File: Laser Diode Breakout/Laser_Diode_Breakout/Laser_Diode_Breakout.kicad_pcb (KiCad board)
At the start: 2 copper layers, 29.2 x 35.6 mm, 8 parts, among them Q1 BSS138, Q2 BSS138

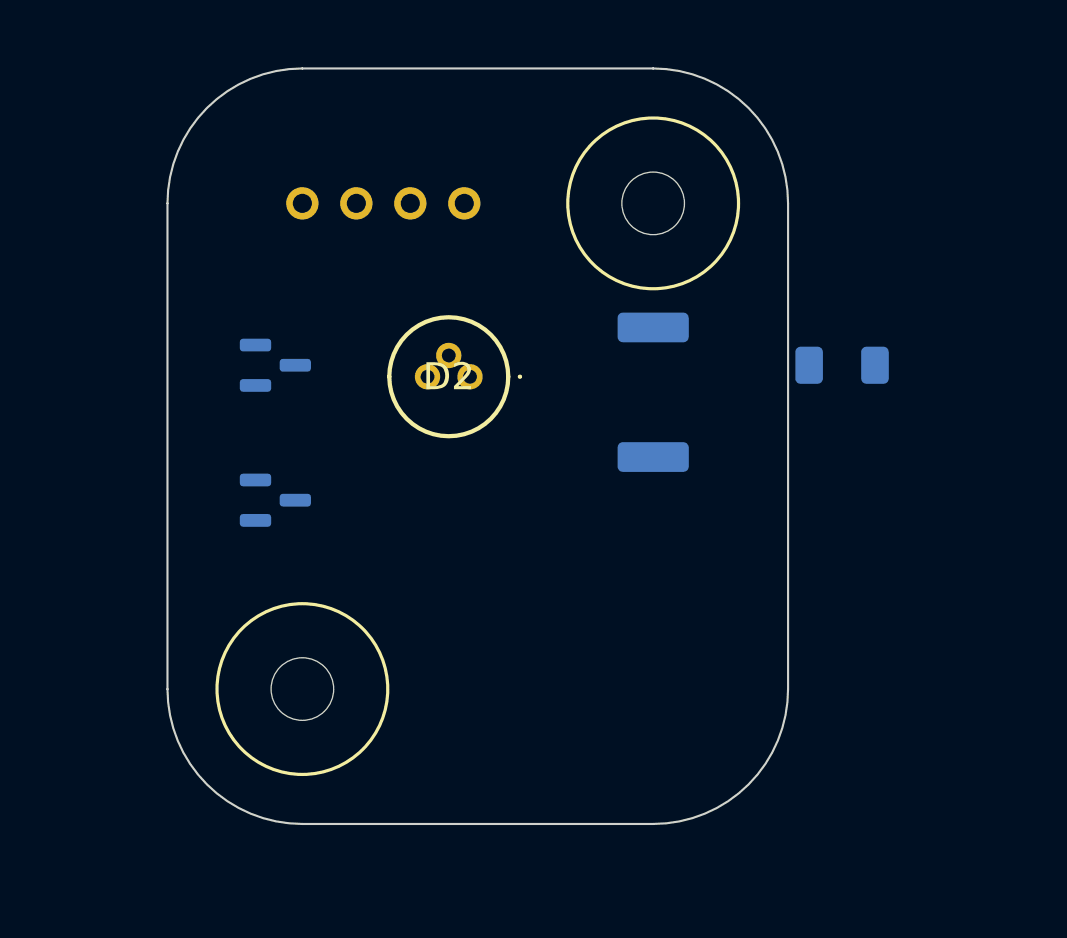
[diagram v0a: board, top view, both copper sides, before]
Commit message: finished adding footprints to laser diode breakout
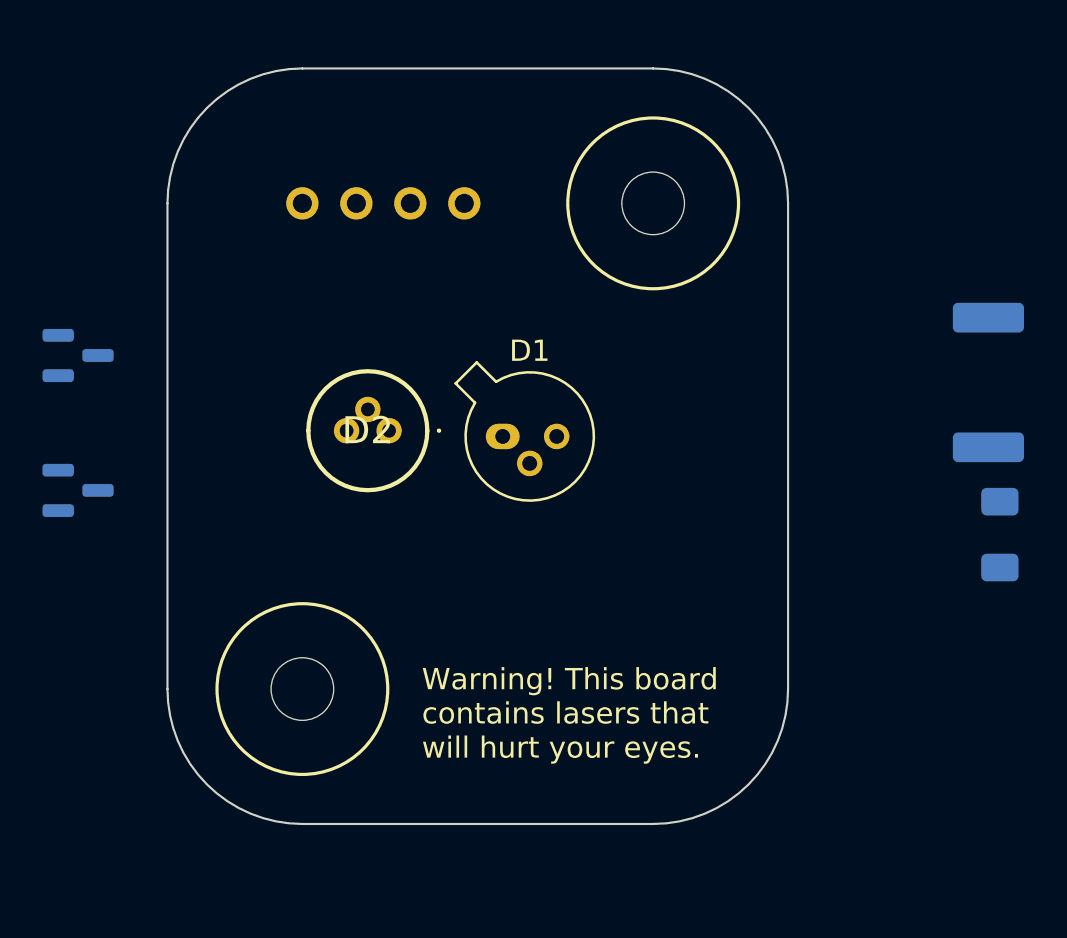
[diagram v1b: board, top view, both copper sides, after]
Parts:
- added D1: 785nm Laser Diode, Package_TO_SOT_THT:TO-18-3, F.Cu at (45.7, 47.0)
- moved R1 15.8 mm to (68.6, 44.5)
- moved R2 10.9 mm to (69.1, 51.6), turned to -90 degrees
- moved Q1 9.30 mm to (25.7, 43.2)
- moved Q2 9.30 mm to (25.7, 49.5)
- moved D2 4.58 mm to (40.4, 46.7)
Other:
- board text added: "Warning! This board contains lasers that will hurt your eyes."
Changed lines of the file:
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@@
   (net 7 "Net-(D1-K)")
   (net 8 "Net-(D1-A)")
+  (footprint "Package_TO_SOT_THT:TO-18-3" (layer "F.Cu")
+    (at 45.72 46.99)
+    (descr "TO-18-3")
+    (tags "TO-18-3")
+    (property "Sheetfile" "Laser_Diode_Breakout.kicad_sch")
+    (property "Sheetname" "")
+    (property "ki_description" "Light emitting diode")
+    (property "ki_keywords" "LED diode")
+    (attr through_hole)
+    (fp_text reference "D1" (at 1.27 -4.02) (layer "F.SilkS")
+        (effects (font (size 1 1) (thickness 0.15)))
+    )
+    (fp_text value "785nm Laser Diode" (at -17.78 3.56) (layer "F.Fab")
+        (effects (font (size 1 1) (thickness 0.15)))
+    )
+    (fp_text user "${REFERENCE}" (at 1.27 -4.02) (layer "F.Fab")
+        (effects (font (size 1 1) (thickness 0.15)))
+    )
+    (fp_line (start -2.214448 -2.494499) (end -1.302281 -1.582331)
+      (stroke (width 0.12) (type solid)) (layer "F.SilkS"))
+    (fp_line (start -1.224499 -3.484448) (end -2.214448 -2.494499)
+      (stroke (width 0.12) (type solid)) (layer "F.SilkS"))
+    (fp_line (start -0.312331 -2.572281) (end -1.224499 -3.484448)
+      (stroke (width 0.12) (type solid)) (layer "F.SilkS"))
+    (fp_arc (start -0.312331 -2.572281) (mid 3.405374 2.135551) (end -1.30215 -1.582544)
+      (stroke (width 0.12) (type solid)) (layer "F.SilkS"))
+    (fp_line (start -2.23 -3.5) (end -2.23 3.15)
+      (stroke (width 0.05) (type solid)) (layer "F.CrtYd"))
+    (fp_line (start -2.23 3.15) (end 4.42 3.15)
+      (stroke (width 0.05) (type solid)) (layer "F.CrtYd"))
+    (fp_line (start 4.42 -3.5) (end -2.23 -3.5)
+      (stroke (width 0.05) (type solid)) (layer "F.CrtYd"))
+    (fp_line (start 4.42 3.15) (end 4.42 -3.5)
+      (stroke (width 0.05) (type solid)) (layer "F.CrtYd"))
+    (fp_line (start -1.976616 -2.426372) (end -1.149301 -1.599057)
+      (stroke (width 0.1) (type solid)) (layer "F.Fab"))
+    (fp_line (start -1.156372 -3.246616) (end -1.976616 -2.426372)
+      (stroke (width 0.1) (type solid)) (layer "F.Fab"))
+    (fp_line (start -0.329057 -2.419301) (end -1.156372 -3.246616)
+      (stroke (width 0.1) (type solid)) (layer "F.Fab"))
+    (fp_arc (start -0.329057 -2.419301) (mid 3.321076 2.050143) (end -1.150029 -1.597956)
+      (stroke (width 0.1) (type solid)) (layer "F.Fab"))
+    (fp_circle (center 1.27 0) (end 3.67 0)
+      (stroke (width 0.1) (type solid)) (fill none) (layer "F.Fab"))
+    (pad "1" thru_hole oval (at 0 0) (size 1.6 1.2) (drill 0.7) (layers "*.Cu" "*.Mask")
+      (net 7 "Net-(D1-K)") (pinfunction "K") (pintype "passive"))
+    (pad "2" thru_hole oval (at 1.27 1.27) (size 1.2 1.2) (drill 0.7) (layers "*.Cu" "*.Mask")
+      (net 8 "Net-(D1-A)") (pinfunction "A") (pintype "passive"))
+    (pad "3" thru_hole oval (at 2.54 0) (size 1.2 1.2) (drill 0.7) (layers "*.Cu" "*.Mask"))
+    (model "${KICAD6_3DMODEL_DIR}/Package_TO_SOT_THT.3dshapes/TO-18-3.wrl"
+      (offset (xyz 0 0 0))
+      (scale (xyz 1 1 1))
+      (rotate (xyz 0 0 0))
+    )
+  )
   (footprint "MRDT_Drill_Holes:4_40_Hole" (layer "F.Cu")
     (at 36.29 58.88)
@@
   )
   (footprint "RamanDiodes:PLT5520B - 520nm" (layer "F.Cu")
-    (at 44.18 44.18 180)
+    (at 40.37 46.72 180)
     (descr "PLT5 520B-6")
     (tags "Diode")
@@
   )
   (footprint "Resistor_SMD:R_2512_6332Metric_Pad1.40x3.35mm_HandSolder" (layer "B.Cu")
-    (at 52.8 44.91 90)
+    (at 68.58 44.45 90)
     (descr "Resistor SMD 2512 (6332 Metric), square (rectangular) end terminal, IPC_7351 nominal with elongated pad for handsoldering. (Body size source: IPC-SM-782 page 72, https://www.pcb-3d.com/wordpress/wp-content/uploads/ipc-sm-782a_amendment_1_and_2.pdf), generated with kicad-footprint-generator")
     (tags "resistor handsolder")
@@
   )
   (footprint "Package_TO_SOT_SMD:SOT-23" (layer "B.Cu")
-    (at 35.02 43.64)
+    (at 25.7325 43.18)
     (descr "SOT, 3 Pin (https://www.jedec.org/system/files/docs/to-236h.pdf variant AB), generated with kicad-footprint-generator ipc_gullwing_generator.py")
     (tags "SOT TO_SOT_SMD")
@@
   )
   (footprint "Resistor_SMD:R_1206_3216Metric_Pad1.30x1.75mm_HandSolder" (layer "B.Cu")
-    (at 61.69 43.64 180)
+    (at 69.12 51.61 -90)
     (descr "Resistor SMD 1206 (3216 Metric), square (rectangular) end terminal, IPC_7351 nominal with elongated pad for handsoldering. (Body size source: IPC-SM-782 page 72, https://www.pcb-3d.com/wordpress/wp-content/uploads/ipc-sm-782a_amendment_1_and_2.pdf), generated with kicad-footprint-generator")
     (tags "resistor handsolder")
@@
     (property "ki_keywords" "R res resistor")
     (attr smd)
-    (fp_text reference "R2" (at 0 1.82) (layer "B.SilkS")
-        (effects (font (size 1 1) (thickness 0.15)) (justify mirror))
-    )
-    (fp_text value "78.7" (at 0 -1.82) (layer "B.Fab")
-        (effects (font (size 1 1) (thickness 0.15)) (justify mirror))
-    )
-    (fp_text user "${REFERENCE}" (at 0 0) (layer "B.Fab")
+    (fp_text reference "R2" (at 0 1.82 -270) (layer "B.SilkS")
+        (effects (font (size 1 1) (thickness 0.15)) (justify mirror))
+    )
+    (fp_text value "78.7" (at 0 -1.82 -270) (layer "B.Fab")
+        (effects (font (size 1 1) (thickness 0.15)) (justify mirror))
+    )
+    (fp_text user "${REFERENCE}" (at 0 0 -270) (layer "B.Fab")
         (effects (font (size 0.8 0.8) (thickness 0.12)) (justify mirror))
     )
@@
     (fp_line (start 1.6 0.8) (end 1.6 -0.8)
       (stroke (width 0.1) (type solid)) (layer "B.Fab"))
-    (pad "1" smd roundrect (at -1.55 0 180) (size 1.3 1.75) (layers "B.Cu" "B.Paste" "B.Mask") (roundrect_rratio 0.192308)
+    (pad "1" smd roundrect (at -1.55 0 270) (size 1.3 1.75) (layers "B.Cu" "B.Paste" "B.Mask") (roundrect_rratio 0.192308)
       (net 1 "+12V") (pintype "passive"))
-    (pad "2" smd roundrect (at 1.55 0 180) (size 1.3 1.75) (layers "B.Cu" "B.Paste" "B.Mask") (roundrect_rratio 0.192308)
+    (pad "2" smd roundrect (at 1.55 0 270) (size 1.3 1.75) (layers "B.Cu" "B.Paste" "B.Mask") (roundrect_rratio 0.192308)
       (net 8 "Net-(D1-A)") (pintype "passive"))
     (model "${KICAD6_3DMODEL_DIR}/Resistor_SMD.3dshapes/R_1206_3216Metric.wrl"
@@
   )
   (footprint "Package_TO_SOT_SMD:SOT-23" (layer "B.Cu")
-    (at 35.02 49.99)
+    (at 25.7325 49.53)
     (descr "SOT, 3 Pin (https://www.jedec.org/system/files/docs/to-236h.pdf variant AB), generated with kicad-footprint-generator ipc_gullwing_generator.py")
     (tags "SOT TO_SOT_SMD")
@@
   (gr_line (start 52.8 29.67) (end 36.29 29.67)
     (stroke (width 0.1) (type default)) (layer "Edge.Cuts"))
+  (gr_text "Warning! This board\ncontains lasers that\nwill hurt your eyes." (at 41.91 62.23) (layer "F.SilkS")
+    (effects (font (size 1 1) (thickness 0.15)) (justify left bottom))
+  )
 )

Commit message: finish diode breakout
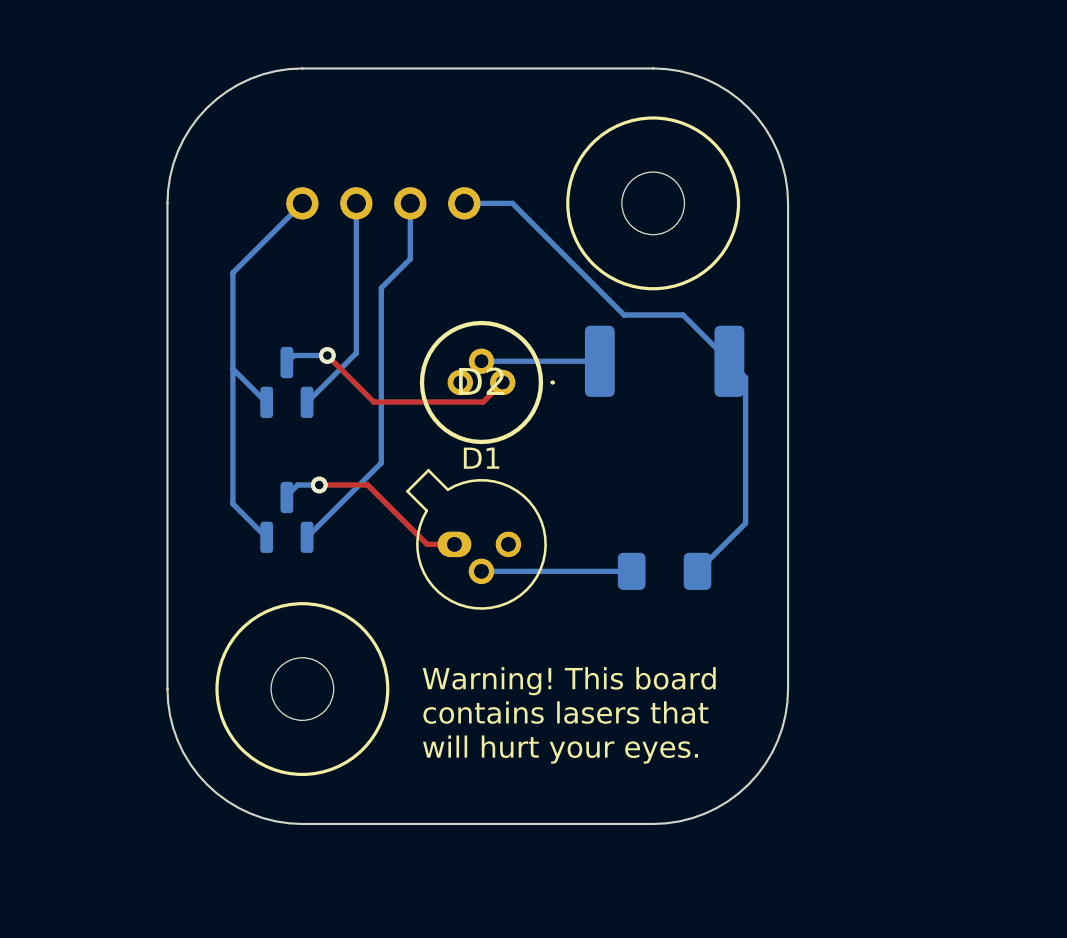
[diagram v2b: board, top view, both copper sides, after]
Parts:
- moved R2 15.9 mm to (53.3, 53.3), turned to 180 degrees
- moved R1 15.3 mm to (53.3, 43.5), turned to 180 degrees
- moved Q1 9.91 mm to (35.6, 44.5), turned to 90 degrees
- moved Q2 9.91 mm to (35.6, 50.8), turned to 90 degrees
- moved D2 5.81 mm to (45.7, 44.5)
- moved D1 5.56 mm to (43.4, 52.1)
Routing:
- net +12V: track 0.00 -> 26.7 mm
- net GND: track 0.00 -> 20.0 mm
- net Red_LED: track 0.00 -> 17.7 mm
- net Net-(D2-K): track 0.00 -> 11.6 mm, vias 0 -> 1
- net Green_LED: track 0.00 -> 10.3 mm
- net Net-(D1-K): track 0.00 -> 9.34 mm, vias 0 -> 1
- net Net-(D1-A): track 0.00 -> 7.07 mm
- net Net-(D2-A): track 0.00 -> 5.57 mm
